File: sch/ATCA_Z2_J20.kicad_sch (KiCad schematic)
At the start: 1 part, among them J18 TE_64690XX-1_J20

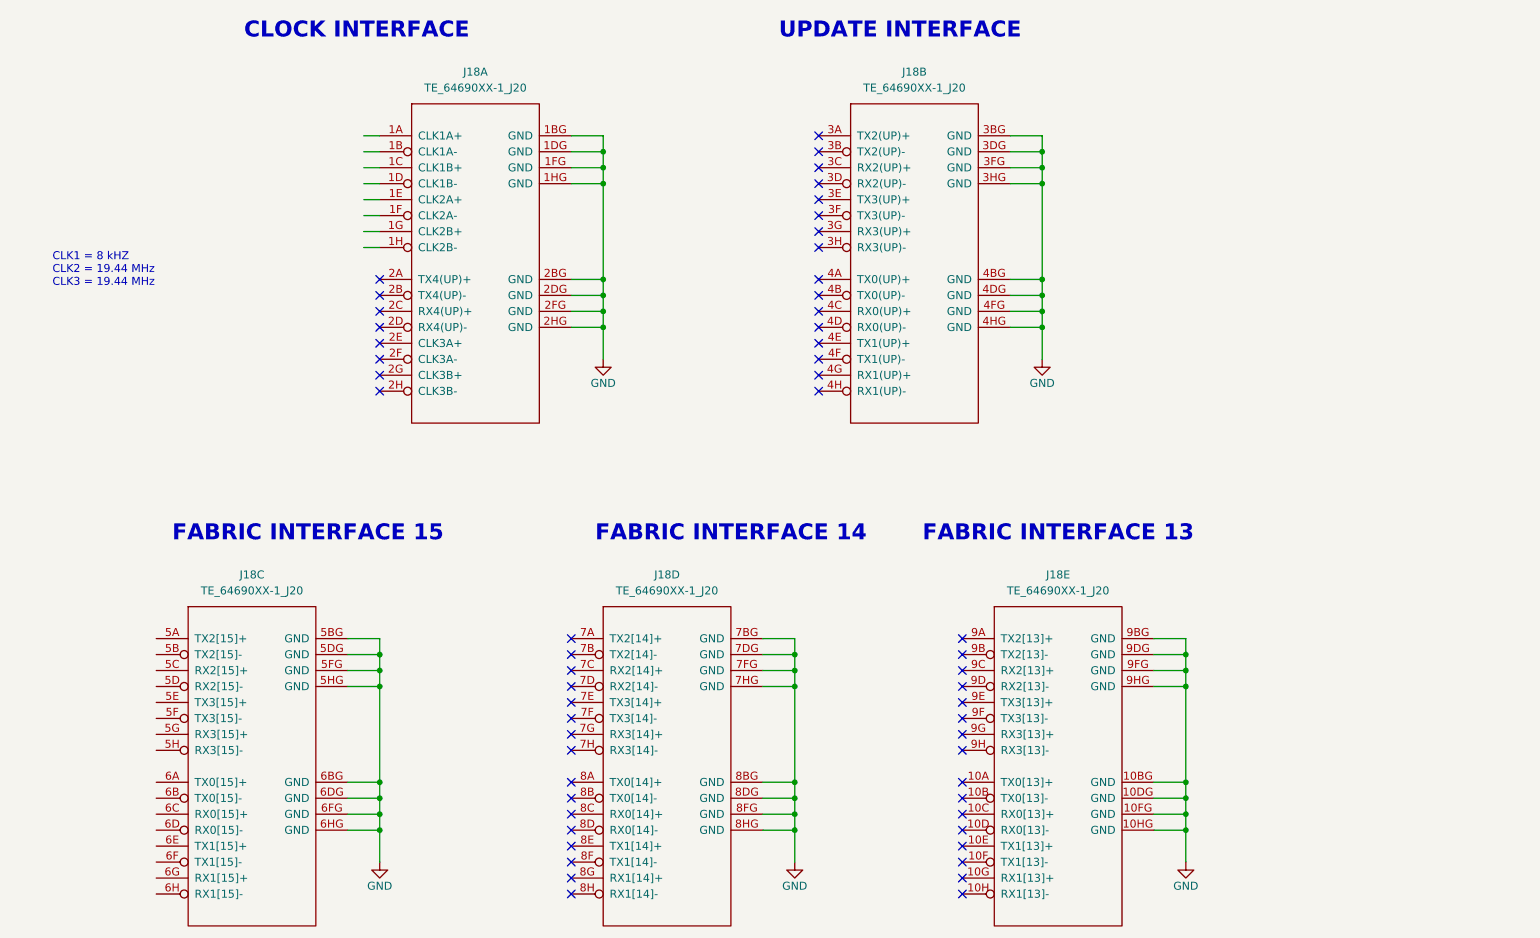
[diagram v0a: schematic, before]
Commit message: added magjacks
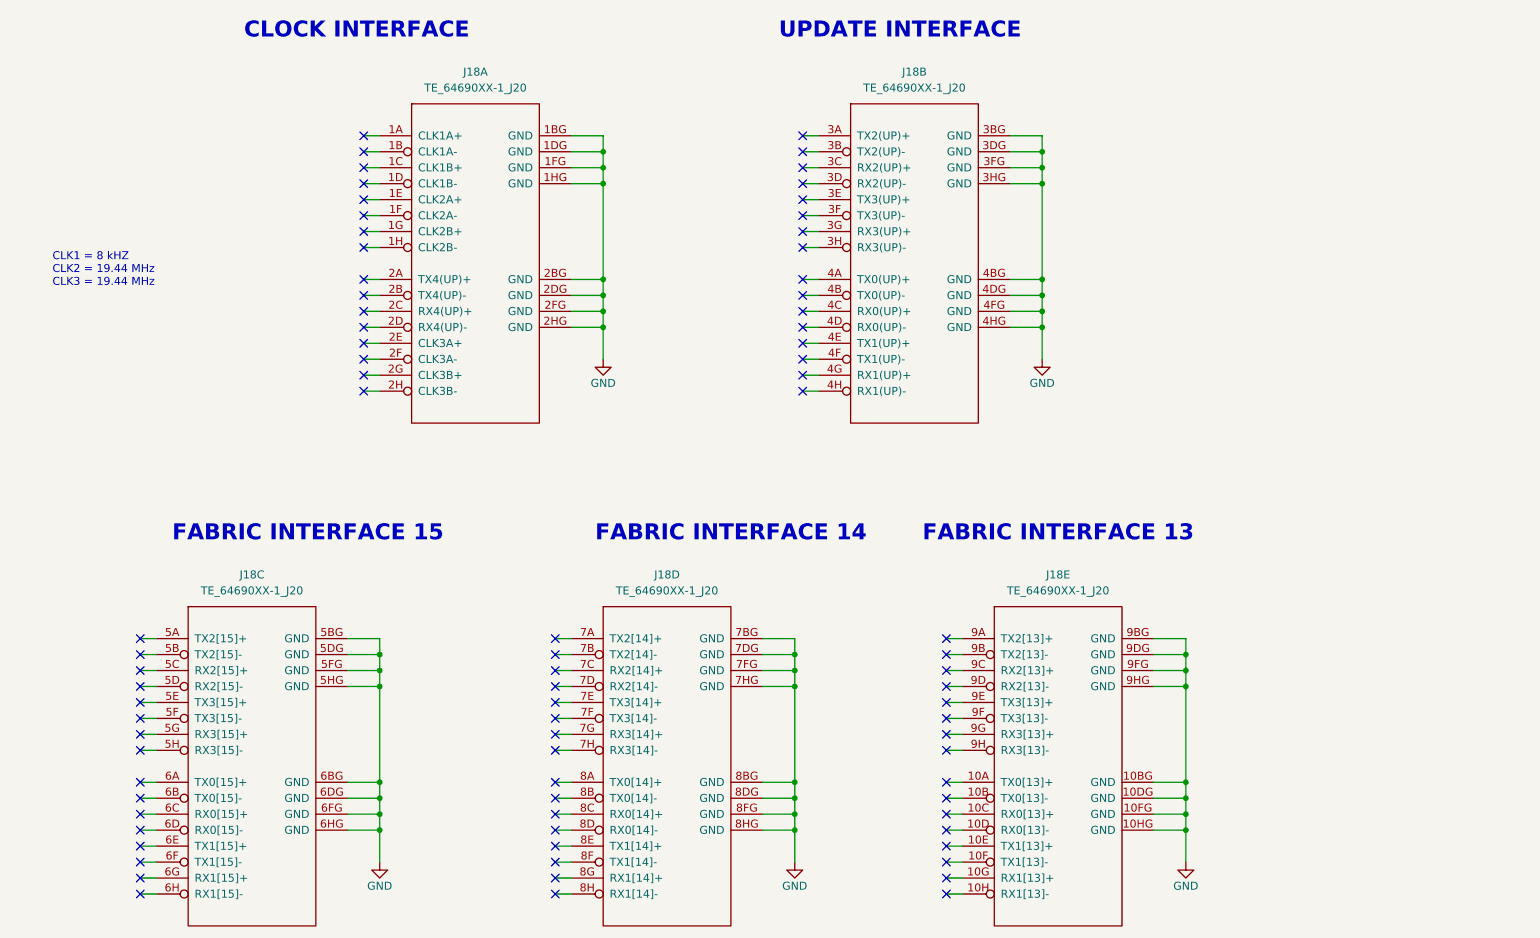
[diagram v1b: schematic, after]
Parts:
- J18: footprint KIT_Connector:TE_6469001-1 -> project:TE_6469001-1
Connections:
- no-connect marks 56 -> 80

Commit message: Project recovered
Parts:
- renumbered J18 to J20
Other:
- title: ATCA Template -> ATCA Simple Loopback HUB
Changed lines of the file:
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@@
   (paper "A4")
   (title_block
-    (title "ATCA Template")
-    (date "2023-07-20")
+    (title "ATCA Simple Loopback HUB")
+    (date "2023-09-12")
     (rev "1.0")
     (company "Karlsruhe Institute of Technology (KIT)")
     (comment 1 "Institute for Data Processing and Electronics (IPE)")
     (comment 2 "Luis Ardila")
-    (comment 4 "Licensed under CERN-OHL-S-2.0")
+    (comment 3 "IPE-380-06")
+    (comment 4 "Licensed under CERN-OHL-P-2.0")
   )
   (junction (at 106.68 116.84) (diameter 0) (color 0 0 0 0)
@@
   (symbol (lib_id "power:GND") (at 142.24 69.85 0) (unit 1)
     (in_bom yes) (on_board yes) (dnp no)
-    (property "Reference" "#PWR01033" (at 142.24 76.2 0)
+    (property "Reference" "#PWR01" (at 142.24 76.2 0)
       (effects (font (size 1.27 1.27)) hide)
     )
@@
     (pin "1")
     (instances
-      (project "atca_simple_hub"
+      (project "atca-simple-loopback-hub"
         (path "/b1bf14e0-f6d2-45a7-b67f-6500a354b7ad/e7c09256-7796-428a-a66f-3a932dc80b14"
           (reference "#PWR01") (unit 1)
@@
   (symbol (lib_name "TE_64690XX-1_J20_4") (lib_id "KIT_Connector:TE_64690XX-1_J20") (at 86.36 134.62 0) (unit 3)
     (in_bom yes) (on_board yes) (dnp no) (fields_autoplaced)
-    (property "Reference" "J18" (at 86.36 104.14 0)
+    (property "Reference" "J20" (at 86.36 104.14 0)
       (effects (font (size 1.27 1.27)))
     )
@@
     (pin "9HG")
     (instances
-      (project "atca_simple_hub"
+      (project "atca-simple-loopback-hub"
         (path "/b1bf14e0-f6d2-45a7-b67f-6500a354b7ad/e7c09256-7796-428a-a66f-3a932dc80b14"
           (reference "J20") (unit 3)
@@
   (symbol (lib_id "power:GND") (at 234.95 149.86 0) (unit 1)
     (in_bom yes) (on_board yes) (dnp no)
-    (property "Reference" "#PWR01036" (at 234.95 156.21 0)
+    (property "Reference" "#PWR018" (at 234.95 156.21 0)
       (effects (font (size 1.27 1.27)) hide)
     )
@@
     (pin "1")
     (instances
-      (project "atca_simple_hub"
+      (project "atca-simple-loopback-hub"
         (path "/b1bf14e0-f6d2-45a7-b67f-6500a354b7ad/e7c09256-7796-428a-a66f-3a932dc80b14"
           (reference "#PWR018") (unit 1)
@@
   (symbol (lib_name "TE_64690XX-1_J20_1") (lib_id "KIT_Connector:TE_64690XX-1_J20") (at 121.92 54.61 0) (unit 1)
     (in_bom yes) (on_board yes) (dnp no) (fields_autoplaced)
-    (property "Reference" "J18" (at 121.92 24.13 0)
+    (property "Reference" "J20" (at 121.92 24.13 0)
       (effects (font (size 1.27 1.27)))
     )
@@
     (pin "9HG")
     (instances
-      (project "atca_simple_hub"
+      (project "atca-simple-loopback-hub"
         (path "/b1bf14e0-f6d2-45a7-b67f-6500a354b7ad/e7c09256-7796-428a-a66f-3a932dc80b14"
           (reference "J20") (unit 1)
@@
   (symbol (lib_id "power:GND") (at 172.72 149.86 0) (unit 1)
     (in_bom yes) (on_board yes) (dnp no)
-    (property "Reference" "#PWR01037" (at 172.72 156.21 0)
+    (property "Reference" "#PWR09" (at 172.72 156.21 0)
       (effects (font (size 1.27 1.27)) hide)
     )
@@
     (pin "1")
     (instances
-      (project "atca_simple_hub"
+      (project "atca-simple-loopback-hub"
         (path "/b1bf14e0-f6d2-45a7-b67f-6500a354b7ad/e7c09256-7796-428a-a66f-3a932dc80b14"
           (reference "#PWR09") (unit 1)
@@
   (symbol (lib_id "power:GND") (at 106.68 149.86 0) (unit 1)
     (in_bom yes) (on_board yes) (dnp no)
-    (property "Reference" "#PWR01034" (at 106.68 156.21 0)
+    (property "Reference" "#PWR04" (at 106.68 156.21 0)
       (effects (font (size 1.27 1.27)) hide)
     )
@@
     (pin "1")
     (instances
-      (project "atca_simple_hub"
+      (project "atca-simple-loopback-hub"
         (path "/b1bf14e0-f6d2-45a7-b67f-6500a354b7ad/e7c09256-7796-428a-a66f-3a932dc80b14"
           (reference "#PWR04") (unit 1)
@@
   (symbol (lib_id "power:GND") (at 212.09 69.85 0) (unit 1)
     (in_bom yes) (on_board yes) (dnp no)
-    (property "Reference" "#PWR01035" (at 212.09 76.2 0)
+    (property "Reference" "#PWR02" (at 212.09 76.2 0)
       (effects (font (size 1.27 1.27)) hide)
     )
@@
     (pin "1")
     (instances
-      (project "atca_simple_hub"
+      (project "atca-simple-loopback-hub"
         (path "/b1bf14e0-f6d2-45a7-b67f-6500a354b7ad/e7c09256-7796-428a-a66f-3a932dc80b14"
           (reference "#PWR02") (unit 1)
@@
   (symbol (lib_name "TE_64690XX-1_J20_3") (lib_id "KIT_Connector:TE_64690XX-1_J20") (at 152.4 134.62 0) (unit 4)
     (in_bom yes) (on_board yes) (dnp no) (fields_autoplaced)
-    (property "Reference" "J18" (at 152.4 104.14 0)
+    (property "Reference" "J20" (at 152.4 104.14 0)
       (effects (font (size 1.27 1.27)))
     )
@@
     (pin "9HG")
     (instances
-      (project "atca_simple_hub"
+      (project "atca-simple-loopback-hub"
         (path "/b1bf14e0-f6d2-45a7-b67f-6500a354b7ad/e7c09256-7796-428a-a66f-3a932dc80b14"
           (reference "J20") (unit 4)
@@
   (symbol (lib_name "TE_64690XX-1_J20_2") (lib_id "KIT_Connector:TE_64690XX-1_J20") (at 191.77 54.61 0) (unit 2)
     (in_bom yes) (on_board yes) (dnp no) (fields_autoplaced)
-    (property "Reference" "J18" (at 191.77 24.13 0)
+    (property "Reference" "J20" (at 191.77 24.13 0)
       (effects (font (size 1.27 1.27)))
     )
@@
     (pin "9HG")
     (instances
-      (project "atca_simple_hub"
+      (project "atca-simple-loopback-hub"
         (path "/b1bf14e0-f6d2-45a7-b67f-6500a354b7ad/e7c09256-7796-428a-a66f-3a932dc80b14"
           (reference "J20") (unit 2)
@@
   (symbol (lib_id "KIT_Connector:TE_64690XX-1_J20") (at 214.63 134.62 0) (unit 5)
     (in_bom yes) (on_board yes) (dnp no) (fields_autoplaced)
-    (property "Reference" "J18" (at 214.63 104.14 0)
+    (property "Reference" "J20" (at 214.63 104.14 0)
       (effects (font (size 1.27 1.27)))
     )
@@
     (pin "9HG")
     (instances
-      (project "atca_simple_hub"
+      (project "atca-simple-loopback-hub"
         (path "/b1bf14e0-f6d2-45a7-b67f-6500a354b7ad/e7c09256-7796-428a-a66f-3a932dc80b14"
           (reference "J20") (unit 5)

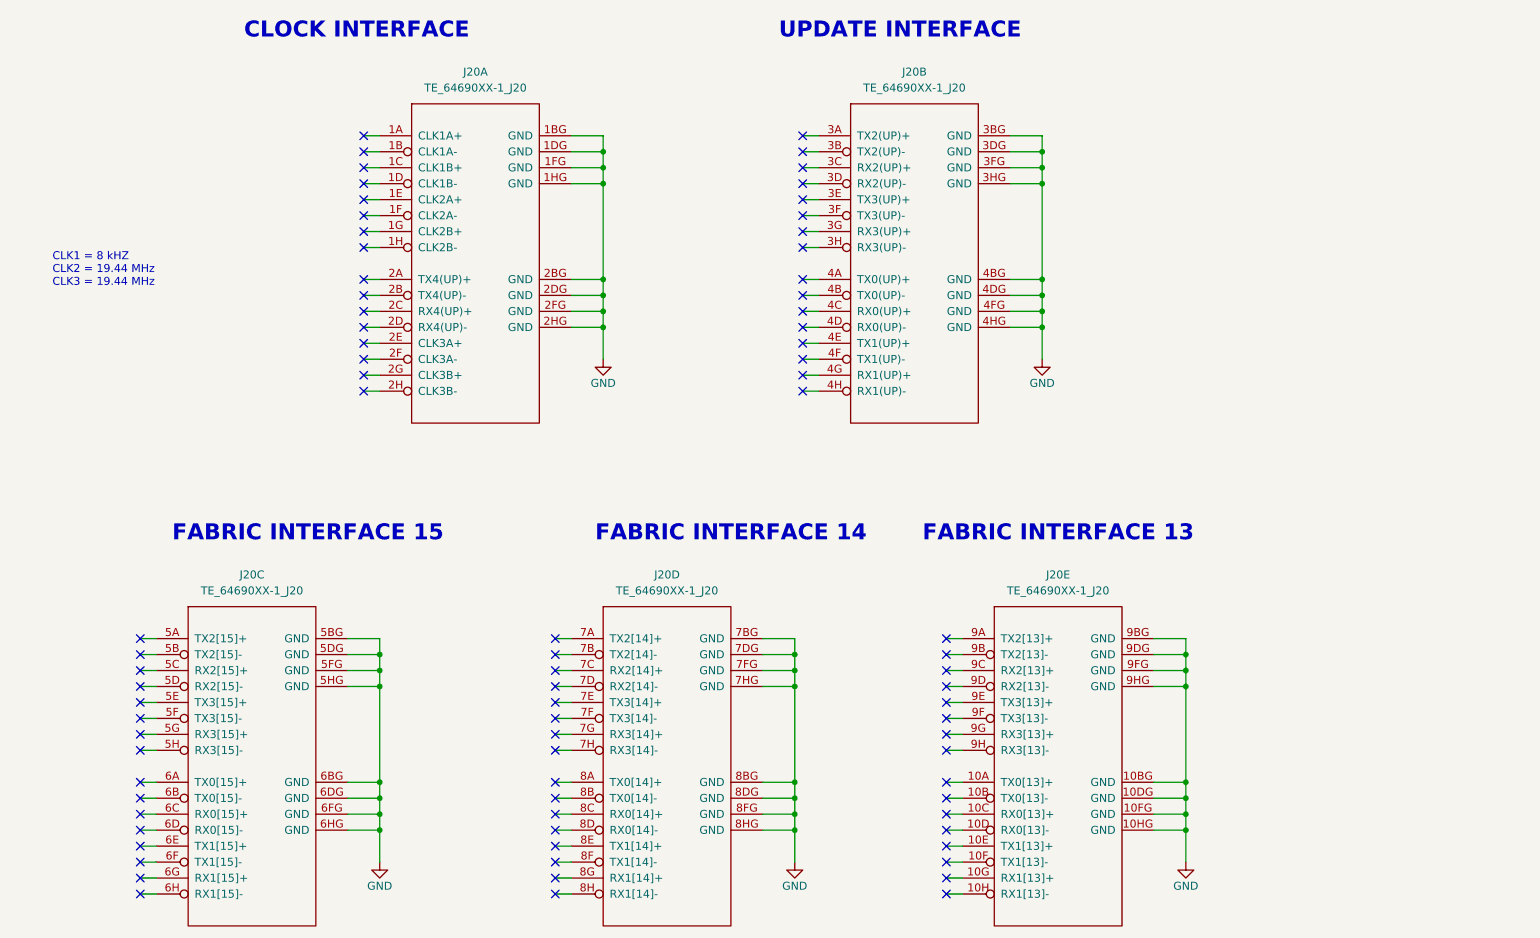
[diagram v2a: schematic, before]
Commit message: organization of sub sheets
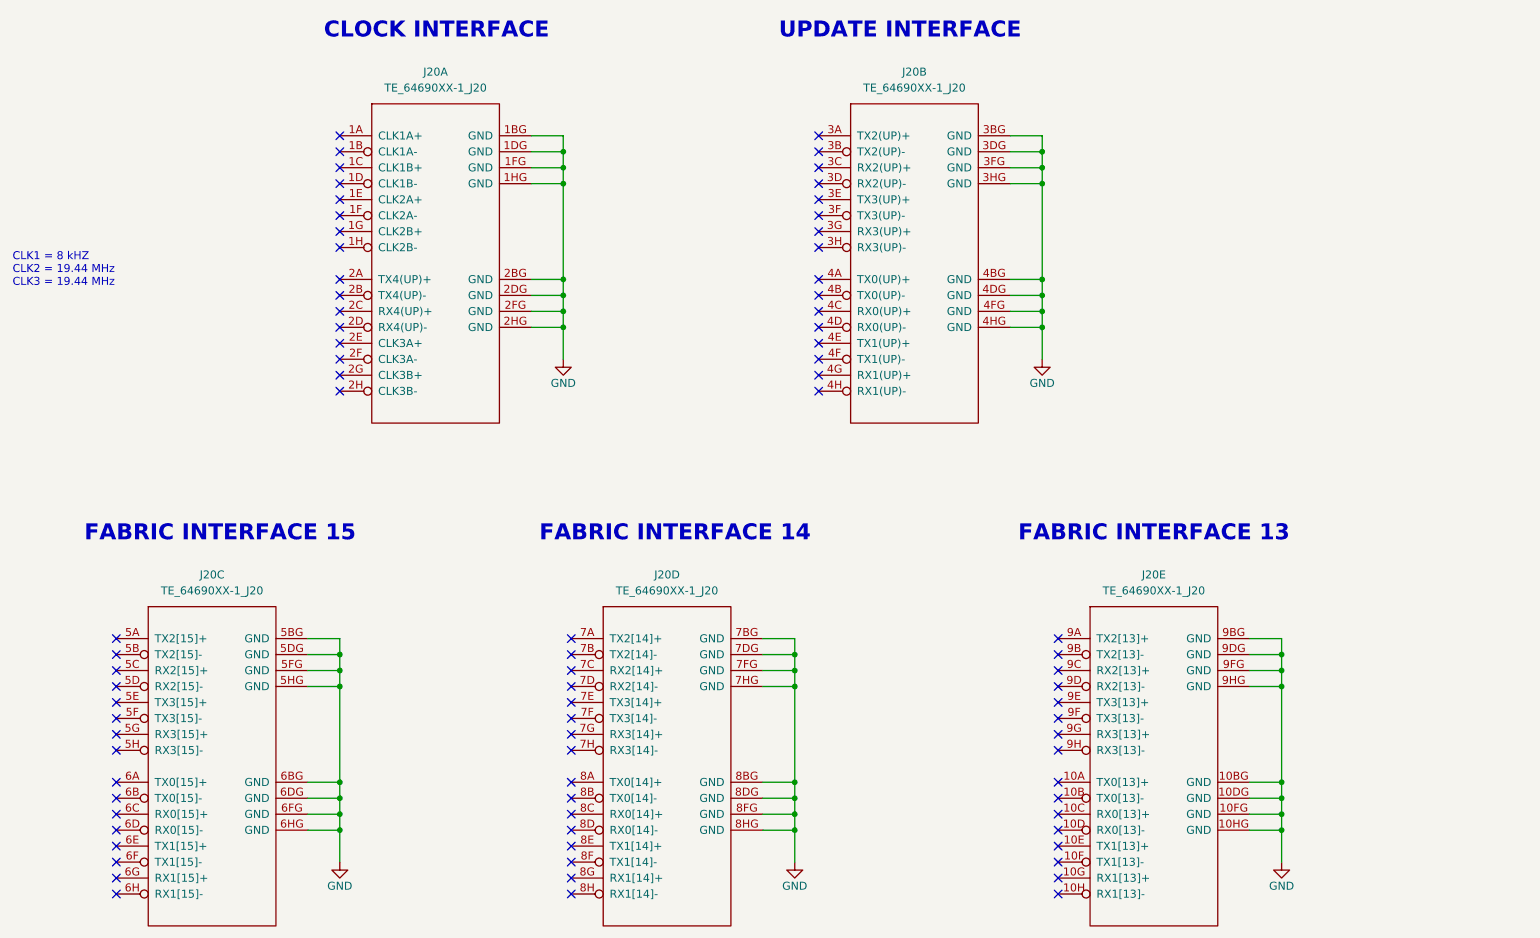
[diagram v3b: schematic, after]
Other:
- moved on the sheet: J20A, J20C, J20E

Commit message: BI and FI
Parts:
- J20: symbol KIT_Connector:TE_64690XX-1_J20 -> project:TE_64690XX-1_J20_4
- J20: symbol KIT_Connector:TE_64690XX-1_J20 -> project:TE_64690XX-1_J20_1
- J20: symbol KIT_Connector:TE_64690XX-1_J20 -> project:TE_64690XX-1_J20_3
- J20: symbol KIT_Connector:TE_64690XX-1_J20 -> project:TE_64690XX-1_J20_2
- J20: symbol KIT_Connector:TE_64690XX-1_J20 -> project:TE_64690XX-1_J20
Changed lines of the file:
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@@
     )
   )
-  (symbol (lib_name "TE_64690XX-1_J20_4") (lib_id "KIT_Connector:TE_64690XX-1_J20") (at 80.01 134.62 0) (unit 3)
+  (symbol (lib_name "TE_64690XX-1_J20_4") (lib_id "project:TE_64690XX-1_J20_4") (at 80.01 134.62 0) (unit 3)
     (in_bom yes) (on_board yes) (dnp no) (fields_autoplaced)
     (property "Reference" "J20" (at 80.01 104.14 0)
@@
     )
   )
-  (symbol (lib_name "TE_64690XX-1_J20_1") (lib_id "KIT_Connector:TE_64690XX-1_J20") (at 115.57 54.61 0) (unit 1)
+  (symbol (lib_name "TE_64690XX-1_J20_1") (lib_id "project:TE_64690XX-1_J20_1") (at 115.57 54.61 0) (unit 1)
     (in_bom yes) (on_board yes) (dnp no) (fields_autoplaced)
     (property "Reference" "J20" (at 115.57 24.13 0)
@@
     )
   )
-  (symbol (lib_name "TE_64690XX-1_J20_3") (lib_id "KIT_Connector:TE_64690XX-1_J20") (at 152.4 134.62 0) (unit 4)
+  (symbol (lib_name "TE_64690XX-1_J20_3") (lib_id "project:TE_64690XX-1_J20_3") (at 152.4 134.62 0) (unit 4)
     (in_bom yes) (on_board yes) (dnp no) (fields_autoplaced)
     (property "Reference" "J20" (at 152.4 104.14 0)
@@
     )
   )
-  (symbol (lib_name "TE_64690XX-1_J20_2") (lib_id "KIT_Connector:TE_64690XX-1_J20") (at 191.77 54.61 0) (unit 2)
+  (symbol (lib_name "TE_64690XX-1_J20_2") (lib_id "project:TE_64690XX-1_J20_2") (at 191.77 54.61 0) (unit 2)
     (in_bom yes) (on_board yes) (dnp no) (fields_autoplaced)
     (property "Reference" "J20" (at 191.77 24.13 0)
@@
     )
   )
-  (symbol (lib_id "KIT_Connector:TE_64690XX-1_J20") (at 229.87 134.62 0) (unit 5)
+  (symbol (lib_id "project:TE_64690XX-1_J20") (at 229.87 134.62 0) (unit 5)
     (in_bom yes) (on_board yes) (dnp no) (fields_autoplaced)
     (property "Reference" "J20" (at 229.87 104.14 0)
